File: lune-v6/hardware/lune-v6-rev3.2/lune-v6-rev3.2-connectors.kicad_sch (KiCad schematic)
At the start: 20 parts, among them J20 ONEWIRE DAISY CHAIN

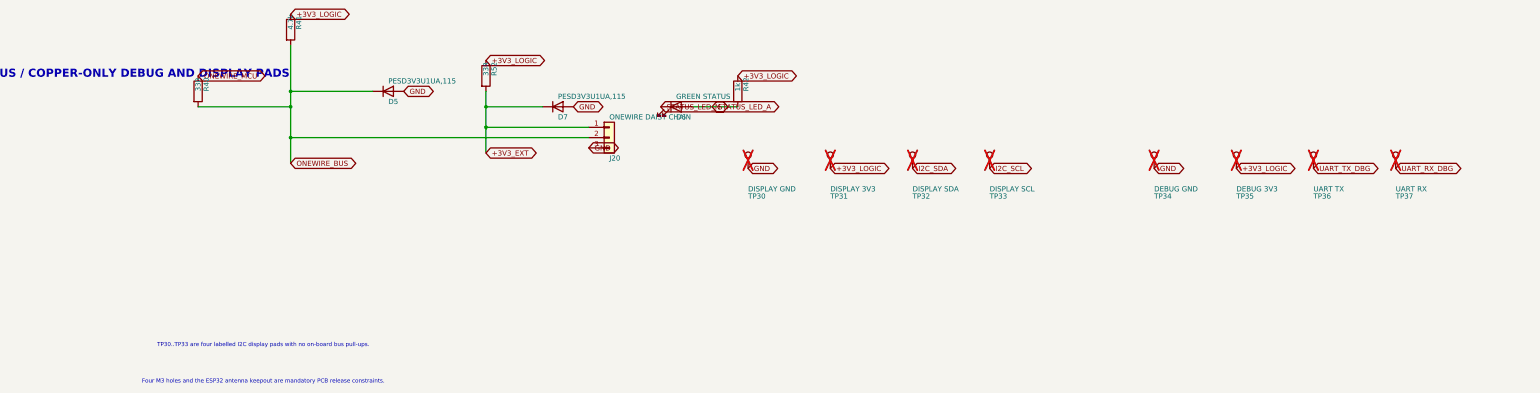
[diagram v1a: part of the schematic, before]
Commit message: Add placement floorplan SVG and geometry JSON for Lune V6 rev3.2
- Introduced a new SVG file for the component placement floorplan, detailing the layout and dimensions of the Lune V6 rev3.2 hardware.
- Added a JSON file containing the geometric coordinates for each component, including reference designators and their respective positions on the board.
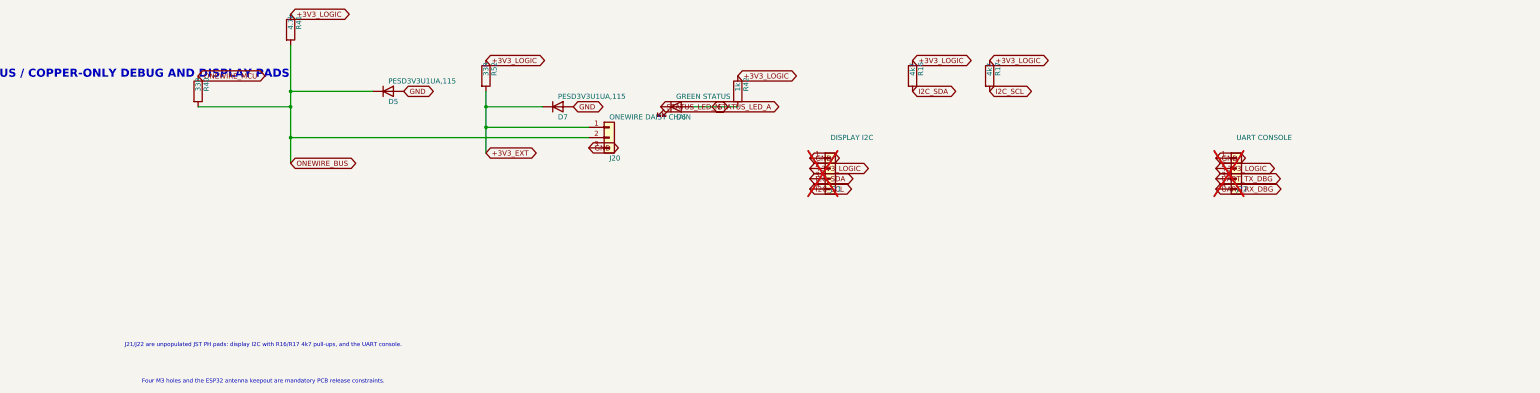
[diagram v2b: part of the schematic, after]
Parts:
- removed TP30: DISPLAY GND, TestPoint:TestPoint_Pad_D1.0mm, symbol Connector:TestPoint
- removed TP31: DISPLAY 3V3, TestPoint:TestPoint_Pad_D1.0mm, symbol Connector:TestPoint
- removed TP32: DISPLAY SDA, TestPoint:TestPoint_Pad_D1.0mm, symbol Connector:TestPoint
- removed TP33: DISPLAY SCL, TestPoint:TestPoint_Pad_D1.0mm, symbol Connector:TestPoint
- removed TP34: DEBUG GND, TestPoint:TestPoint_Pad_D1.0mm, symbol Connector:TestPoint
- removed TP35: DEBUG 3V3, TestPoint:TestPoint_Pad_D1.0mm, symbol Connector:TestPoint
- removed TP36: UART TX, TestPoint:TestPoint_Pad_D1.0mm, symbol Connector:TestPoint
- removed TP37: UART RX, TestPoint:TestPoint_Pad_D1.0mm, symbol Connector:TestPoint
- added J21: DISPLAY I2C, Connector_JST:JST_XH_B4B-XH-A_1x04_P2.50mm_Vertical, symbol Connector_Generic:Conn_01x04
- added J22: UART CONSOLE, Connector_JST:JST_XH_B4B-XH-A_1x04_P2.50mm_Vertical, symbol Connector_Generic:Conn_01x04
- added R16, R17: 4k7, Resistor_SMD:R_0603_1608Metric, symbol Device:R
- H1, H2, H3, H4: footprint MountingHole:MountingHole_3.2mm_M3 -> MountingHole:MountingHole_3.2mm_M3_ISO14580_Pad
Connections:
- net +3V3_LOGIC: now also J21.2 (Pin_2), J22.2 (Pin_2), R16.1, R17.1
- net GND: now also J21.1 (Pin_1), J22.1 (Pin_1)
- net I2C_SCL: now also J21.4 (Pin_4), R17.2
- net I2C_SDA: now also J21.3 (Pin_3), R16.2
- net UART_RX_DBG: now also J22.4 (Pin_4)
- net UART_TX_DBG: now also J22.3 (Pin_3)
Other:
- note added: "J21/J22 are unpopulated JST PH pads: display I2C with R16/R17 4k7 pull-ups, and the UART console."
- note removed: "TP30..TP33 are four labelled I2C display pads with no on-board bus pull-ups."
